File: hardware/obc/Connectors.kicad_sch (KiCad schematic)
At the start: 28 parts, among them J101 Conn_02x20_Odd_Even, J301 USB_C_Receptacle_USB2.0, J302 Conn_High-Rel_4S2P_Vertical, J303 Conn_01x06, J304 Conn_High-Rel_6P, U301 Mem_MT29F4G01ABAFDWB

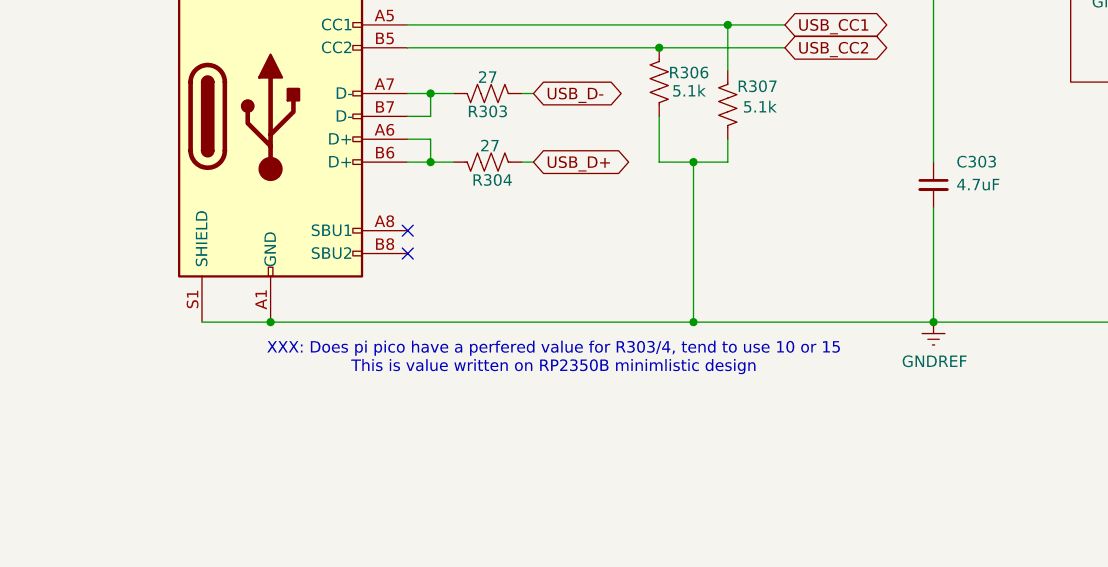
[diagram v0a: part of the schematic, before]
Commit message: OBC: Continuing work towards the next revision
- Cleaned up text on Avionics Page
- Changed some descriptions and cleaned up text on Power Page
- Changed Power Relay A schematic to one from PCB
- Changed R120 and R401 changed from 107k to 34.8k and changed R121 and R404 from 0 to 10k and R127 and R419 from 3.01k to 3.83k (Solar Chargers Page)
- Checked R303 and R304 resistor value and believe 27 is correct
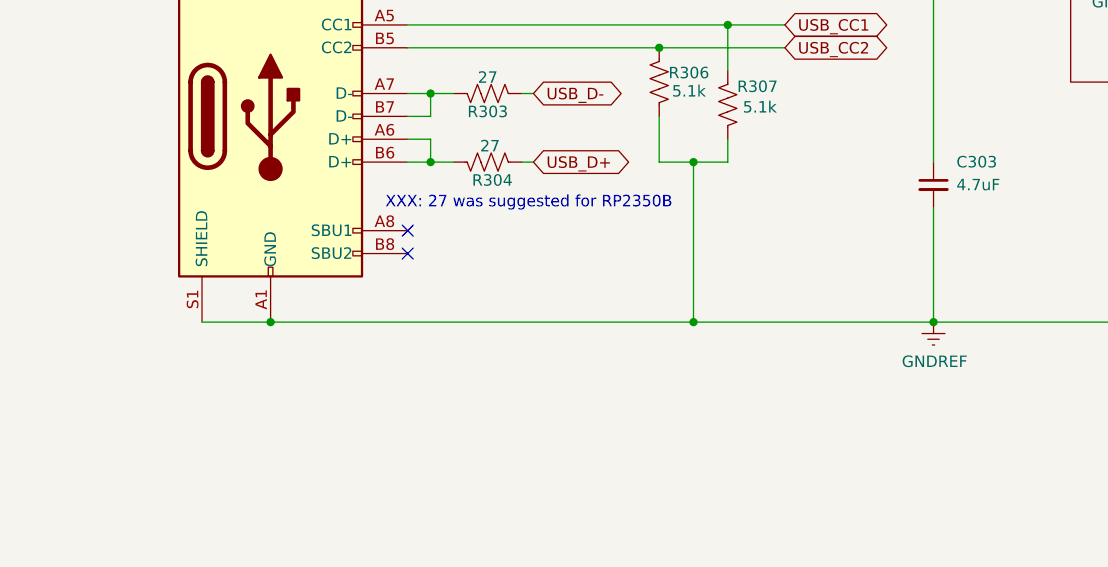
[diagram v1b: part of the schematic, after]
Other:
- note added: "XXX: 27 was suggested for RP2350B"
- note removed: "XXX: Does pi pico have a perfered value for R303/4, tend to use 10 or 15 This is value written on RP2350B minimlistic design"
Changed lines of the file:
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@@
 		)
 	)
-	(text "XXX: Does pi pico have a perfered value for R303/4, tend to use 10 or 15\nThis is value written on RP2350B minimlistic design"
+	(text "XXX: 27 was suggested for RP2350B"
 		(exclude_from_sim no)
-		(at 89.916 87.884 0)
+		(at 87.122 70.612 0)
 		(effects
 			(font

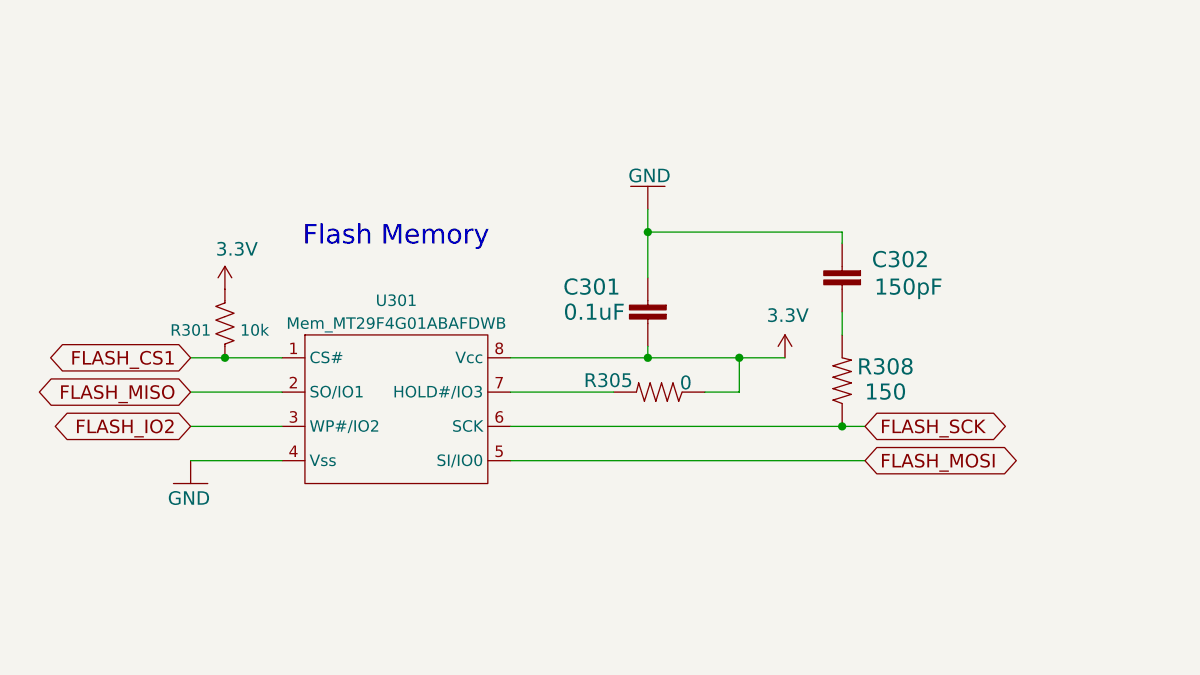
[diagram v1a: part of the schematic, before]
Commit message: obc: changed flash memory to PSRAM
- Fixed MRAM symbol
- Removed Flash memory for new PSRAM
- Changed labels on Avionics page to match format
- Added another 0.1uF capacitor to VRAG pins
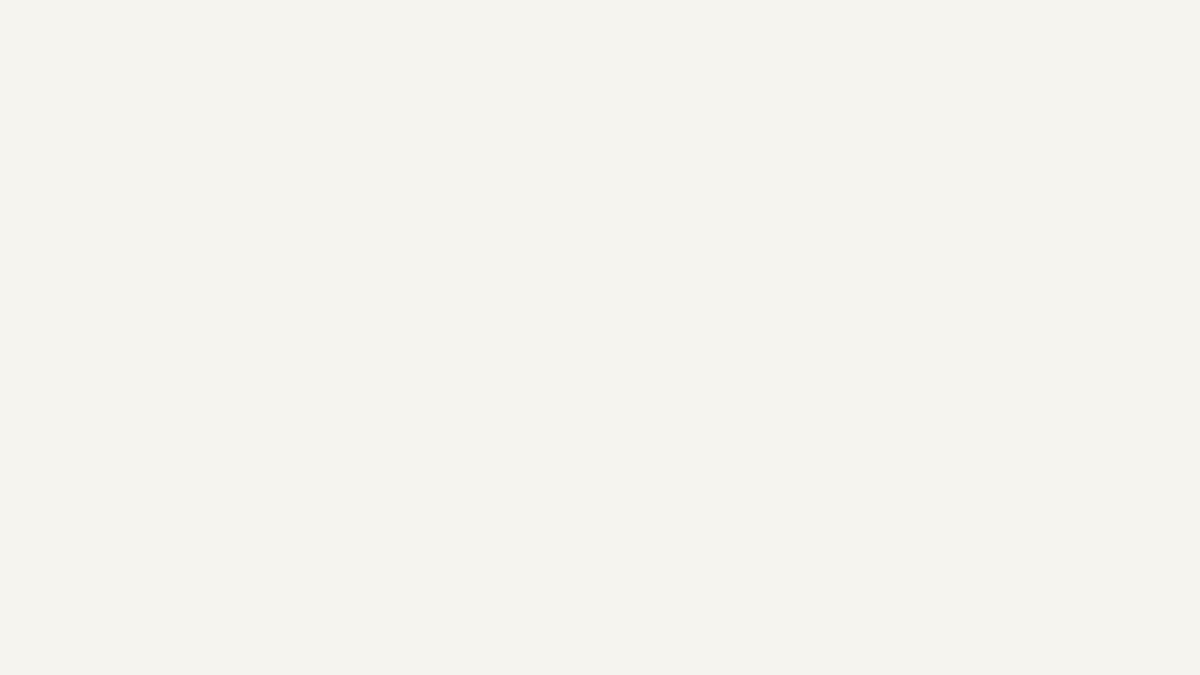
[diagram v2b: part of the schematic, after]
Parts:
- removed C301: 0.1uF, Capacitor_SMD:C_0603_1608Metric, symbol mainboard:2.2UF-0603-10V-20%
- removed C302: 150pF, Capacitor_SMD:C_0603_1608Metric, symbol mainboard:2.2UF-0603-10V-20%
- removed R301: 10k, Resistor_SMD:R_0603_1608Metric, symbol Device:R_US
- removed R305: 0, Resistor_SMD:R_0603_1608Metric, symbol mainboard:RESISTOR0603
- removed R308: 150, Resistor_SMD:R_0603_1608Metric, symbol mainboard:RESISTOR0603
- removed U301: Mem_MT29F4G01ABAFDWB, SSE_Footprints:UPDFN-8_8.0x6.0mm_P1.27mm, symbol SSE_Symbols:Mem_MT29F4G01ABAFDWB
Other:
- note removed: "Flash Memory"

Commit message: obc: Fixed errors from design review
- Gave proper attribution on all pages
- Spread out components on Avionics page
- Changed GPS power circuit
- Added a DNP resistor in between VBATT and VWATCHEDRAIL
- Added various other part numbers on Power Supervisor and Watch Dog Page
- Changed Power Supervisor and Watch Dog Page to page 3
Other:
- company: Ruchir Kavulli, Michael Lyle -> Ruchir Kavulli, Luke Titi, Michael Lyle
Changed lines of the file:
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@@
 		(date "2024-06-07")
 		(rev "1")
-		(company "Ruchir Kavulli, Michael Lyle")
+		(company "Ruchir Kavulli, Luke Titi, Michael Lyle")
 		(comment 1 "Derived from PyCubed Mainboard v5")
 	)

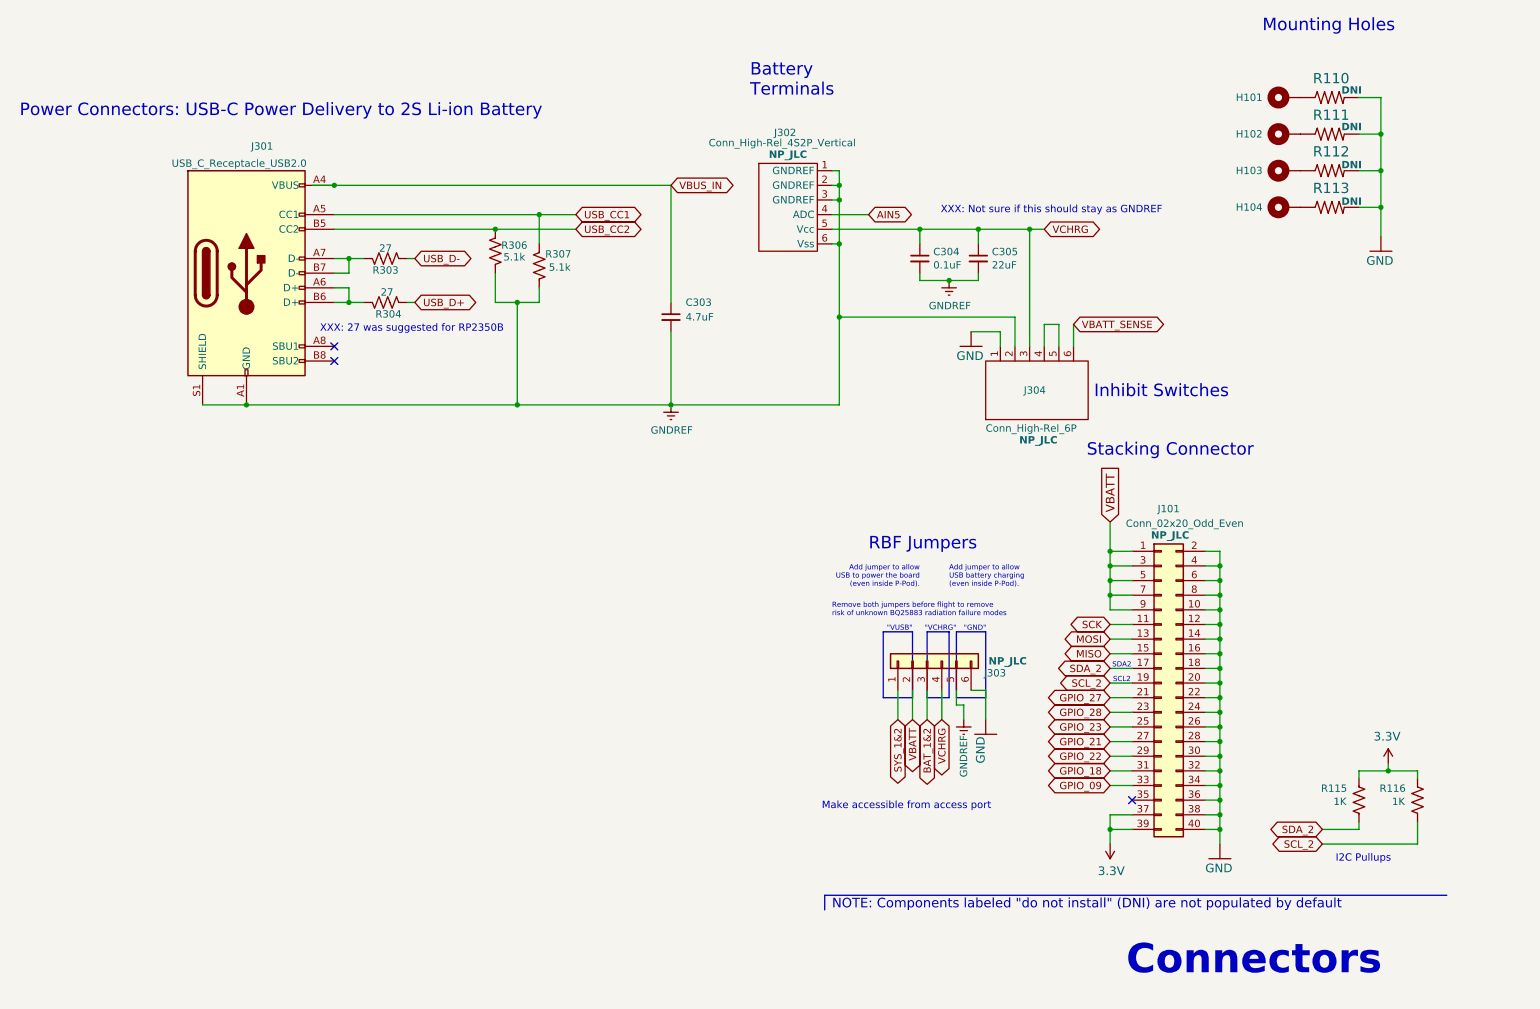
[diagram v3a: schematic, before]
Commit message: obc: Fixed second design review, and fixed up BOM
- added layout comments on schematic
- fixed various comments
- added many LCSC # for components
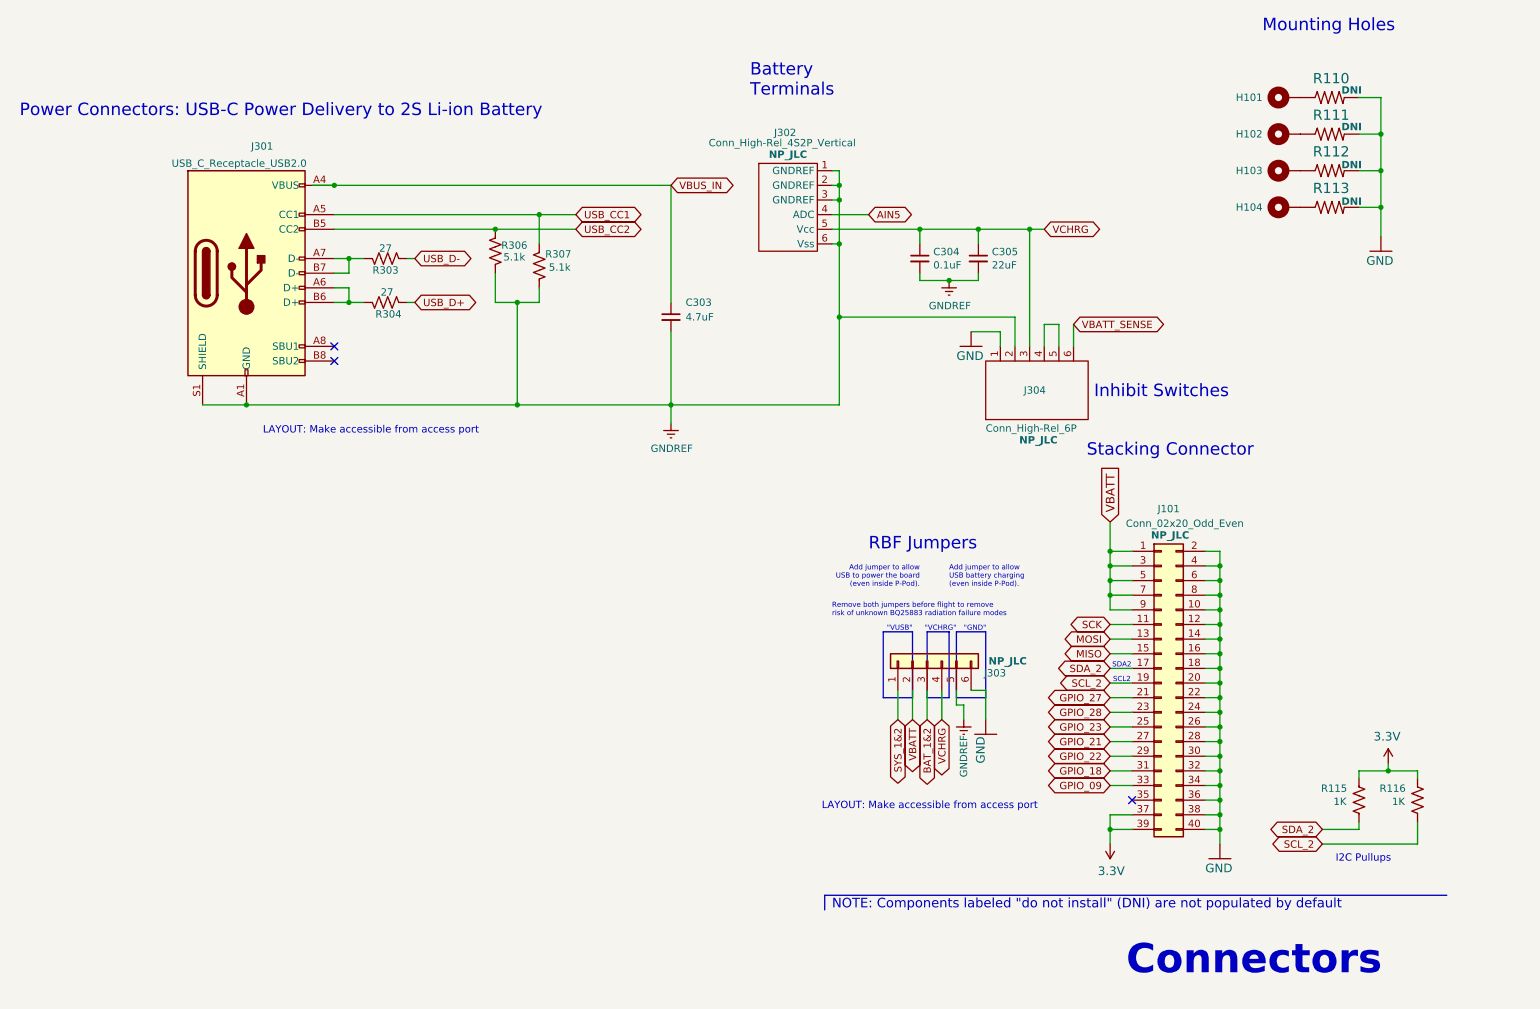
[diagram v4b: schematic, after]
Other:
- note added: "LAYOUT: Make accessible from access port"
- note removed: "Make accessible from access port"
- note removed: "XXX: 27 was suggested for RP2350B"
- note removed: "XXX: Not sure if this should stay as GNDREF"
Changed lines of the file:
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@@
 	(wire
 		(pts
+			(xy 132.08 86.995) (xy 132.08 83.82)
+		)
+		(stroke
+			(width 0)
+			(type default)
+		)
+	)
+	(wire
+		(pts
 			(xy 255.27 54.61) (xy 255.27 49.53)
 		)
@@
 		)
 	)
-	(text "XXX: Not sure if this should stay as GNDREF"
-		(exclude_from_sim no)
-		(at 198.12 50.038 0)
-		(effects
-			(font
-				(size 1.27 1.27)
-			)
-		)
-	)
 	(text "Add jumper to allow\nUSB battery charging\n(even inside P-Pod).\n"
 		(exclude_from_sim no)
@@
 		)
 	)
-	(text "XXX: 27 was suggested for RP2350B"
-		(exclude_from_sim no)
-		(at 87.122 70.612 0)
-		(effects
-			(font
-				(size 1.27 1.27)
-			)
-		)
-	)
 	(text "Battery\nTerminals"
 		(exclude_from_sim no)
@@
 		)
 	)
-	(text "Make accessible from access port"
+	(text "LAYOUT: Make accessible from access port"
 		(exclude_from_sim no)
 		(at 158.242 154.178 0)
@@
 		)
 	)
+	(text "LAYOUT: Make accessible from access port"
+		(exclude_from_sim no)
+		(at 80.01 88.265 0)
+		(effects
+			(font
+				(size 1.27 1.27)
+			)
+		)
+	)
 	(text "Add jumper to allow\nUSB to power the board\n(even inside P-Pod).\n"
 		(exclude_from_sim no)
@@
 			)
 		)
+		(property "Sim.Type" ""
+			(at 58.42 60.96 0)
+			(effects
+				(font
+					(size 1.27 1.27)
+				)
+				(hide yes)
+			)
+		)
 		(pin "A1"
 		)
@@
 			)
 		)
+		(property "Sim.Type" ""
+			(at 175.26 58.42 0)
+			(effects
+				(font
+					(size 1.27 1.27)
+				)
+				(hide yes)
+			)
+		)
 		(pin "1"
 		)
@@
 			)
 		)
+		(property "Sim.Type" ""
+			(at 185.42 58.42 0)
+			(effects
+				(font
+					(size 1.27 1.27)
+				)
+				(hide yes)
+			)
+		)
 		(pin "1"
 		)
@@
 			)
 		)
+		(property "Sim.Type" ""
+			(at 109.22 59.69 0)
+			(effects
+				(font
+					(size 1.27 1.27)
+				)
+				(hide yes)
+			)
+		)
 		(pin "1"
 		)
@@
 			)
 		)
+		(property "Sim.Type" ""
+			(at 101.6 57.15 0)
+			(effects
+				(font
+					(size 1.27 1.27)
+				)
+				(hide yes)
+			)
+		)
 		(pin "1"
 		)
@@
 			)
 		)
+		(property "Sim.Type" ""
+			(at 132.08 68.58 0)
+			(effects
+				(font
+					(size 1.27 1.27)
+				)
+				(hide yes)
+			)
+		)
 		(pin "1"
 		)
@@
 	(symbol
 		(lib_id "power:GNDREF")
-		(at 132.08 83.82 0)
+		(at 132.08 86.995 0)
 		(unit 1)
 		(exclude_from_sim no)
@@
 		(dnp no)
 		(property "Reference" "#PWR0301"
-			(at 132.08 90.17 0)
+			(at 132.08 93.345 0)
 			(effects
 				(font
@@
 		)
 		(property "Value" "GNDREF"
-			(at 132.207 88.2142 0)
+			(at 132.207 91.3892 0)
 			(effects
 				(font
@@
 		)
 		(property "Footprint" ""
-			(at 132.08 83.82 0)
+			(at 132.08 86.995 0)
 			(effects
 				(font
@@
 		)
 		(property "Datasheet" ""
-			(at 132.08 83.82 0)
+			(at 132.08 86.995 0)
 			(effects
 				(font
@@
 		)
 		(property "Description" ""
-			(at 132.08 83.82 0)
+			(at 132.08 86.995 0)
 			(effects
 				(font
@@
 			)
 		)
+		(property "Sim.Type" ""
+			(at 238.76 30.48 0)
+			(effects
+				(font
+					(size 1.27 1.27)
+				)
+				(hide yes)
+			)
+		)
 		(pin "1"
 		)
@@
 			)
 		)
+		(property "Sim.Type" ""
+			(at 246.38 43.18 0)
+			(effects
+				(font
+					(size 1.27 1.27)
+				)
+				(hide yes)
+			)
+		)
 		(pin "1"
 		)
@@
 			)
 		)
+		(property "Sim.Type" ""
+			(at 246.38 30.48 0)
+			(effects
+				(font
+					(size 1.27 1.27)
+				)
+				(hide yes)
+			)
+		)
 		(pin "1"
 		)
@@
 			)
 		)
+		(property "Sim.Type" ""
+			(at 82.55 58.42 0)
+			(effects
+				(font
+					(size 1.27 1.27)
+				)
+				(hide yes)
+			)
+		)
 		(pin "1"
 		)
@@
 			)
 		)
+		(property "Sim.Type" ""
+			(at 251.46 152.4 0)
+			(effects
+				(font
+					(size 1.27 1.27)
+				)
+				(hide yes)
+			)
+		)
 		(pin "1"
 		)
@@
 			)
 		)
+		(property "Sim.Type" ""
+			(at 238.76 43.18 0)
+			(effects
+				(font
+					(size 1.27 1.27)
+				)
+				(hide yes)
+			)
+		)
 		(pin "1"
 		)
@@
 			)
 		)
+		(property "Sim.Type" ""
+			(at 238.76 49.53 0)
+			(effects
+				(font
+					(size 1.27 1.27)
+				)
+				(hide yes)
+			)
+		)
 		(pin "1"
 		)
@@
 			)
 		)
+		(property "Sim.Type" ""
+			(at 154.94 48.26 0)
+			(effects
+				(font
+					(size 1.27 1.27)
+				)
+				(hide yes)
+			)
+		)
 		(pin "3"
 		)
@@
 			)
 		)
+		(property "Sim.Type" ""
+			(at 246.38 36.83 0)
+			(effects
+				(font
+					(size 1.27 1.27)
+				)
+				(hide yes)
+			)
+		)
 		(pin "1"
 		)
@@
 			)
 		)
+		(property "Sim.Type" ""
+			(at 246.38 49.53 0)
+			(effects
+				(font
+					(size 1.27 1.27)
+				)
+				(hide yes)
+			)
+		)
 		(pin "1"
 		)
@@
 			)
 		)
+		(property "Sim.Type" ""
+			(at 82.55 66.04 0)
+			(effects
+				(font
+					(size 1.27 1.27)
+				)
+				(hide yes)
+			)
+		)
 		(pin "1"
 		)
@@
 			)
 		)
+		(property "Sim.Type" ""
+			(at 238.76 36.83 0)
+			(effects
+				(font
+					(size 1.27 1.27)
+				)
+				(hide yes)
+			)
+		)
 		(pin "1"
 		)
@@
 			)
 		)
+		(property "Sim.Type" ""
+			(at 176.53 128.27 0)
+			(effects
+				(font
+					(size 1.27 1.27)
+				)
+				(hide yes)
+			)
+		)
 		(pin "1"
 		)
@@
 			)
 		)
+		(property "Sim.Type" ""
+			(at 261.62 152.4 0)
+			(effects
+				(font
+					(size 1.27 1.27)
+				)
+				(hide yes)
+			)
+		)
 		(pin "1"
 		)
@@
 			)
 		)
+		(property "Sim.Type" ""
+			(at 217.17 132.08 0)
+			(effects
+				(font
+					(size 1.27 1.27)
+				)
+				(hide yes)
+			)
+		)
 		(pin "1"
 		)
@@
 			)
 		)
+		(property "Sim.Type" ""
+			(at 185.42 80.01 0)
+			(effects
+				(font
+					(size 1.27 1.27)
+				)
+				(hide yes)
+			)
+		)

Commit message: obc: PCB work done towards next revision
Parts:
- R115, R116: value 1K -> 1k
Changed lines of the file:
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@@
 			)
 		)
-		(property "Value" "1K"
+		(property "Value" "1k"
 			(at 248.158 152.654 0)
 			(effects
@@
 			)
 		)
-		(property "Value" "1K"
+		(property "Value" "1k"
 			(at 258.318 152.654 0)
 			(effects
